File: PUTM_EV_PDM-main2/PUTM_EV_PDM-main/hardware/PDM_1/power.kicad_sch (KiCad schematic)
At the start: 21 parts, among them U2 LD1117S33TR_SOT223, U3 LM2675M-5

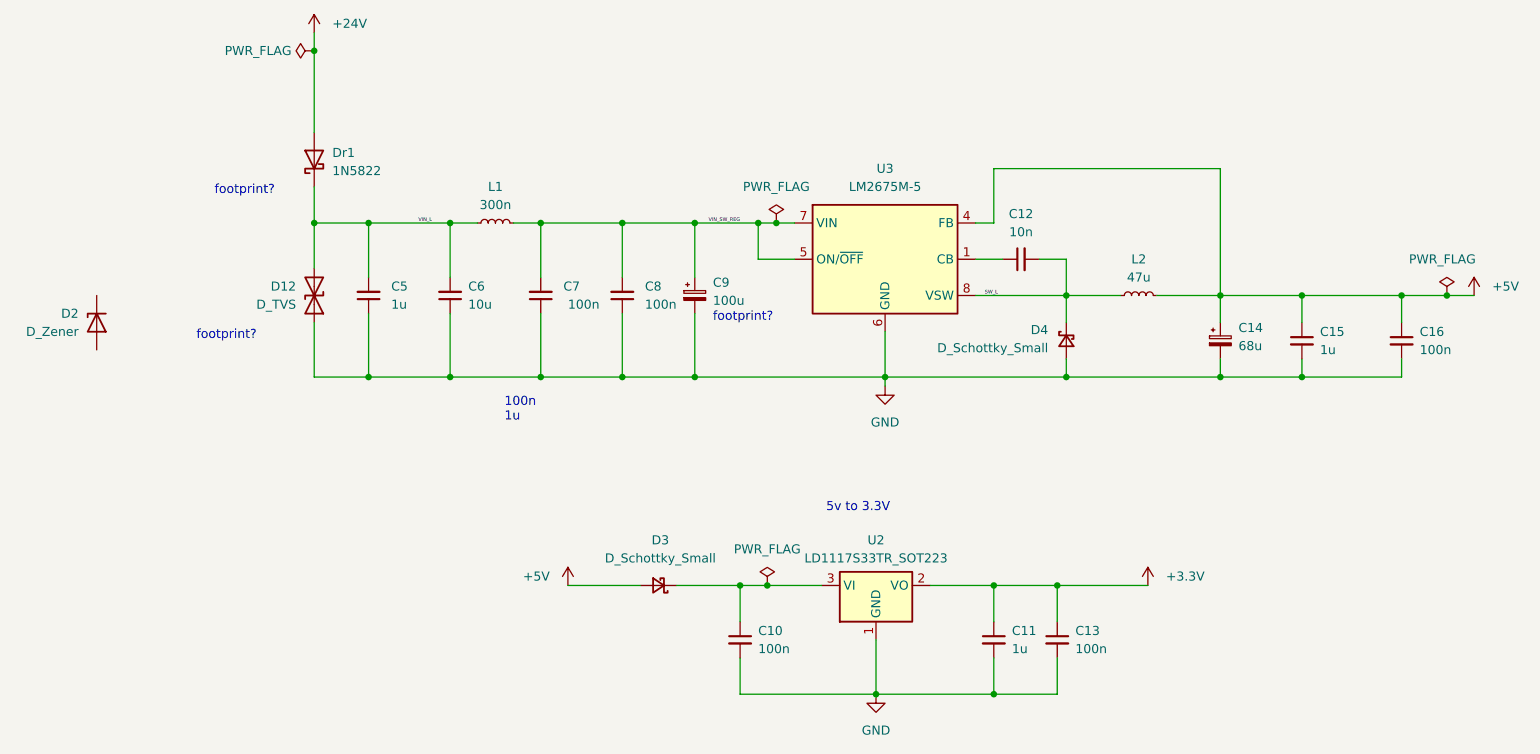
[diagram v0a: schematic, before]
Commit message: lepsze footprinty
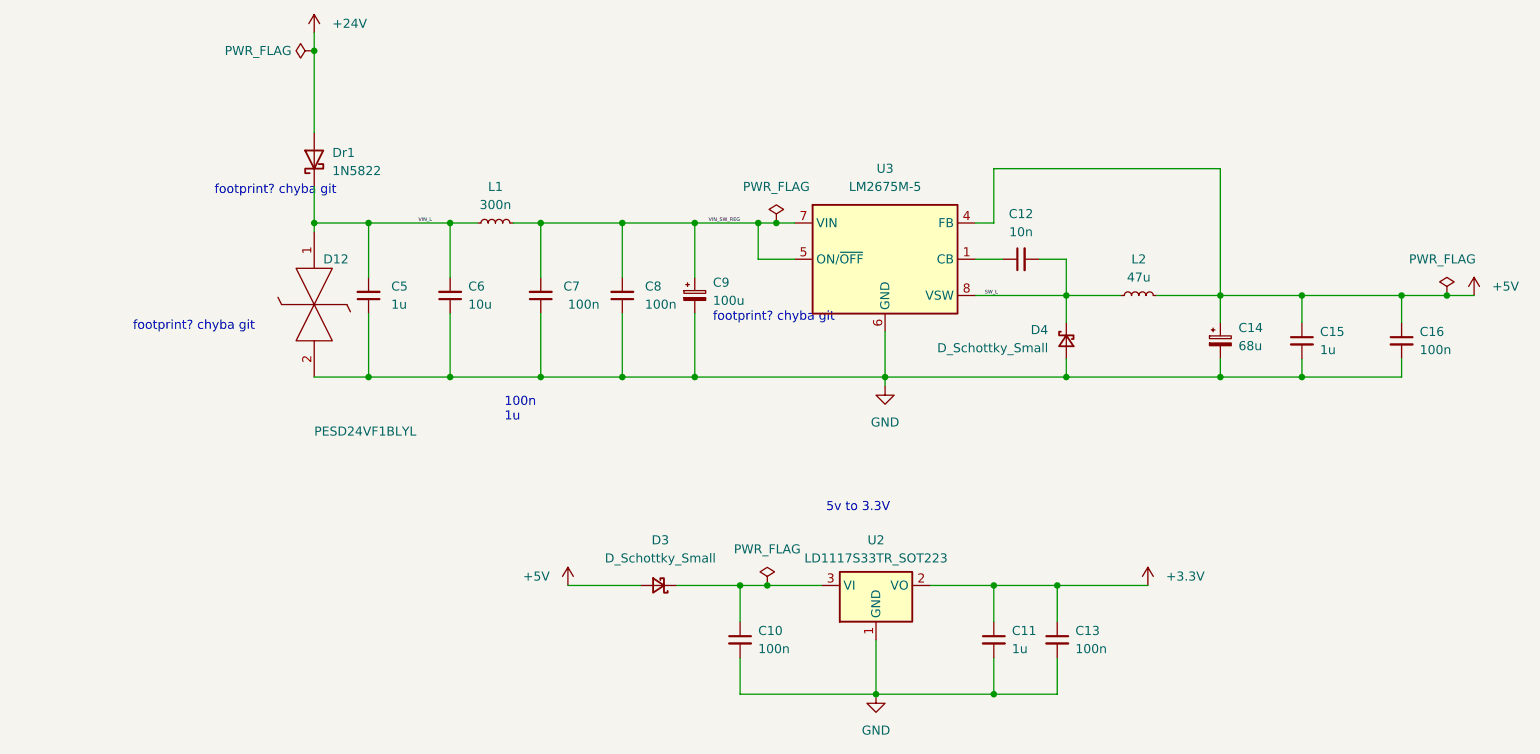
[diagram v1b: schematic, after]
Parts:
- removed D12: D_TVS, Diode_SMD:D_SMA, symbol Device:D_TVS
- removed D2: D_Zener, Diode_SMD:D_SOD-123, symbol Device:D_Zener
- added D12: PESD24VF1BLYL, Diode_SMD:D_SMA, symbol PESD24VF1BLYL:PESD24VF1BLYL
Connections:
- net GND: now also D12.2
- net VIN_L: now also D12.1
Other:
- note added: "footprint? chyba git"
- note removed: "footprint?"
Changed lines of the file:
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@@
   (junction (at 107.95 77.47) (diameter 0) (color 0 0 0 0)
   )
+  (junction (at 154.94 143.51) (diameter 0) (color 0 0 0 0)
+  )
+  (junction (at 129.54 99.06) (diameter 0) (color 0 0 0 0)
+  )
   (junction (at 76.2 77.47) (diameter 0) (color 0 0 0 0)
   )
-  (junction (at 154.94 143.51) (diameter 0) (color 0 0 0 0)
-  )
-  (junction (at 129.54 99.06) (diameter 0) (color 0 0 0 0)
-  )
   (junction (at 107.95 99.06) (diameter 0) (color 0 0 0 0)
   )
@@
     (stroke (width 0) (type default))
   )
+  (wire (pts (xy 76.2 77.47) (xy 76.2 78.74))
+    (stroke (width 0) (type default))
+  )
   (wire (pts (xy 119.38 77.47) (xy 129.54 77.47))
     (stroke (width 0) (type default))
@@
     (stroke (width 0) (type default))
   )
-  (wire (pts (xy 76.2 77.47) (xy 76.2 83.82))
-    (stroke (width 0) (type default))
-  )
   (wire (pts (xy 171.45 128.27) (xy 171.45 133.35))
     (stroke (width 0) (type default))
@@
     (stroke (width 0) (type default))
   )
-  (wire (pts (xy 76.2 91.44) (xy 76.2 99.06))
-    (stroke (width 0) (type default))
-  )
   (wire (pts (xy 83.82 90.17) (xy 83.82 99.06))
     (stroke (width 0) (type default))
@@
     (stroke (width 0) (type default))
   )
-  (text "footprint?" (at 59.69 93.98 0)
+  (text "footprint? chyba git" (at 50.8 92.71 0)
     (effects (font (size 1.27 1.27)) (justify left bottom))
   )
-  (text "footprint?" (at 132.08 91.44 0)
+  (text "footprint? chyba git\n" (at 132.08 91.44 0)
     (effects (font (size 1.27 1.27)) (justify left bottom))
   )
@@
     (effects (font (size 1.27 1.27)) (justify left bottom))
   )
-  (text "footprint?" (at 62.23 73.66 0)
+  (text "footprint? chyba git\n" (at 62.23 73.66 0)
     (effects (font (size 1.27 1.27)) (justify left bottom))
   )
@@
     )
   )
-  (symbol (lib_id "Device:D_Zener") (at 45.72 91.44 90) (mirror x) (unit 1)
+  (symbol (lib_id "power:+24V") (at 76.2 50.8 0) (unit 1)
+    (in_bom yes) (on_board yes) (dnp no) (fields_autoplaced)
+    (property "Reference" "#PWR04" (at 76.2 54.61 0)
+      (effects (font (size 1.27 1.27)) hide)
+    )
+    (property "Value" "+24V" (at 78.74 49.53 0)
+      (effects (font (size 1.27 1.27)) (justify left))
+    )
+    (property "Footprint" "" (at 76.2 50.8 0)
+      (effects (font (size 1.27 1.27)) hide)
+    )
+    (property "Datasheet" "" (at 76.2 50.8 0)
+      (effects (font (size 1.27 1.27)) hide)
+    )
+    (pin "1")
+    (instances
+      (project "PDM_1"
+        (path "/b652b05a-4e3d-4ad1-b032-18886abe7d45/1367ec17-5fee-46da-adec-17b799499894"
+          (reference "#PWR04") (unit 1)
+        )
+      )
+      (project "PDM"
+        (path "/d7434f1a-7415-4eaa-a71b-b9580d7b34f2/bce9111c-7679-44f6-9761-394d41af211c"
+          (reference "#PWR016") (unit 1)
+        )
+      )
+    )
+  )
+  (symbol (lib_id "PESD24VF1BLYL:PESD24VF1BLYL") (at 76.2 78.74 270) (unit 1)
     (in_bom yes) (on_board yes) (dnp no)
-    (property "Reference" "D2" (at 43.18 90.17 90)
-      (effects (font (size 1.27 1.27)) (justify left))
-    )
-    (property "Value" "D_Zener" (at 43.18 92.71 90)
-      (effects (font (size 1.27 1.27)) (justify left))
-    )
-    (property "Footprint" "Diode_SMD:D_SOD-123" (at 45.72 91.44 0)
-      (effects (font (size 1.27 1.27)) hide)
-    )
-    (property "Datasheet" "file:///C:/Users/kacpe/Downloads/1N4728A.PDF" (at 45.72 91.44 0)
-      (effects (font (size 1.27 1.27)) hide)
-    )
-    (pin "1")
-    (pin "2")
-    (instances
-      (project "PDM_1"
-        (path "/b652b05a-4e3d-4ad1-b032-18886abe7d45/1367ec17-5fee-46da-adec-17b799499894"
-          (reference "D2") (unit 1)
-        )
-      )
-      (project "PDM"
-        (path "/d7434f1a-7415-4eaa-a71b-b9580d7b34f2/bce9111c-7679-44f6-9761-394d41af211c"
-          (reference "D6") (unit 1)
-        )
-      )
-    )
-  )
-  (symbol (lib_id "power:+24V") (at 76.2 50.8 0) (unit 1)
-    (in_bom yes) (on_board yes) (dnp no) (fields_autoplaced)
-    (property "Reference" "#PWR04" (at 76.2 54.61 0)
-      (effects (font (size 1.27 1.27)) hide)
-    )
-    (property "Value" "+24V" (at 78.74 49.53 0)
-      (effects (font (size 1.27 1.27)) (justify left))
-    )
-    (property "Footprint" "" (at 76.2 50.8 0)
-      (effects (font (size 1.27 1.27)) hide)
-    )
-    (property "Datasheet" "" (at 76.2 50.8 0)
-      (effects (font (size 1.27 1.27)) hide)
-    )
-    (pin "1")
-    (instances
-      (project "PDM_1"
-        (path "/b652b05a-4e3d-4ad1-b032-18886abe7d45/1367ec17-5fee-46da-adec-17b799499894"
-          (reference "#PWR04") (unit 1)
-        )
-      )
-      (project "PDM"
-        (path "/d7434f1a-7415-4eaa-a71b-b9580d7b34f2/bce9111c-7679-44f6-9761-394d41af211c"
-          (reference "#PWR016") (unit 1)
+    (property "Reference" "D12" (at 77.47 82.55 90)
+      (effects (font (size 1.27 1.27)) (justify left))
+    )
+    (property "Value" "PESD24VF1BLYL" (at 76.2 106.68 90)
+      (effects (font (size 1.27 1.27)) (justify left))
+    )
+    (property "Footprint" "Diode_SMD:D_SMA" (at 80.01 93.98 0)
+      (effects (font (size 1.27 1.27)) (justify left bottom) hide)
+    )
+    (property "Datasheet" "https://assets.nexperia.com/documents/data-sheet/PESD24VF1BL.pdf" (at 77.47 93.98 0)
+      (effects (font (size 1.27 1.27)) (justify left bottom) hide)
+    )
+    (property "Description" "PESD24VF1BL - Ultra low capacitance bidirectional ESD protection diode" (at 74.93 93.98 0)
+      (effects (font (size 1.27 1.27)) (justify left bottom) hide)
+    )
+    (property "Height" "0" (at 72.39 93.98 0)
+      (effects (font (size 1.27 1.27)) (justify left bottom) hide)
+    )
+    (property "Mouser Part Number" "771-PESD24VF1BLYL" (at 69.85 93.98 0)
+      (effects (font (size 1.27 1.27)) (justify left bottom) hide)
+    )
+    (property "Mouser Price/Stock" "https://www.mouser.co.uk/ProductDetail/Nexperia/PESD24VF1BLYL?qs=M%2FOdCRO8QQ2u4QQQVkgemw%3D%3D" (at 67.31 93.98 0)
+      (effects (font (size 1.27 1.27)) (justify left bottom) hide)
+    )
+    (property "Manufacturer_Name" "Nexperia" (at 64.77 93.98 0)
+      (effects (font (size 1.27 1.27)) (justify left bottom) hide)
+    )
+    (property "Manufacturer_Part_Number" "PESD24VF1BLYL" (at 62.23 93.98 0)
+      (effects (font (size 1.27 1.27)) (justify left bottom) hide)
+    )
+    (pin "1")
+    (pin "2")
+    (instances
+      (project "PDM_1"
+        (path "/b652b05a-4e3d-4ad1-b032-18886abe7d45/1367ec17-5fee-46da-adec-17b799499894"
+          (reference "D12") (unit 1)
         )
       )
@@
     )
   )
-  (symbol (lib_id "Device:D_TVS") (at 76.2 87.63 270) (mirror x) (unit 1)
-    (in_bom yes) (on_board yes) (dnp no)
-    (property "Reference" "D12" (at 73.66 86.36 90)
-      (effects (font (size 1.27 1.27)) (justify right))
-    )
-    (property "Value" "D_TVS" (at 73.66 88.9 90)
-      (effects (font (size 1.27 1.27)) (justify right))
-    )
-    (property "Footprint" "Diode_SMD:D_SMA" (at 76.2 87.63 0)
-      (effects (font (size 1.27 1.27)) hide)
-    )
-    (property "Datasheet" "~" (at 76.2 87.63 0)
-      (effects (font (size 1.27 1.27)) hide)
-    )
-    (pin "1")
-    (pin "2")
-    (instances
-      (project "PDM_1"
-        (path "/b652b05a-4e3d-4ad1-b032-18886abe7d45/1367ec17-5fee-46da-adec-17b799499894"
-          (reference "D12") (unit 1)
-        )
-      )
-    )
-  )
   (symbol (lib_id "power:PWR_FLAG") (at 76.2 53.34 90) (unit 1)
     (in_bom yes) (on_board yes) (dnp no) (fields_autoplaced)
@@
       (effects (font (size 1.27 1.27)) hide)
     )
-    (property "Datasheet" "http://www.vishay.com/docs/88526/1n5820.pdf" (at 76.2 68.58 0)
-      (effects (font (size 1.27 1.27)) hide)
-    )
+    (property "Datasheet" "https://www.mouser.pl/ProductDetail/Taiwan-Semiconductor/SS34ALH?qs=A6eO%252BMLsxmQip%2FrgNup6RA%3D%3D" (at 76.2 68.58 0)
+      (effects (font (size 1.27 1.27)) hide)
+    )

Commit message: nowe połączenia
dodane połączenia z STM
dodane złącza
dodane LED
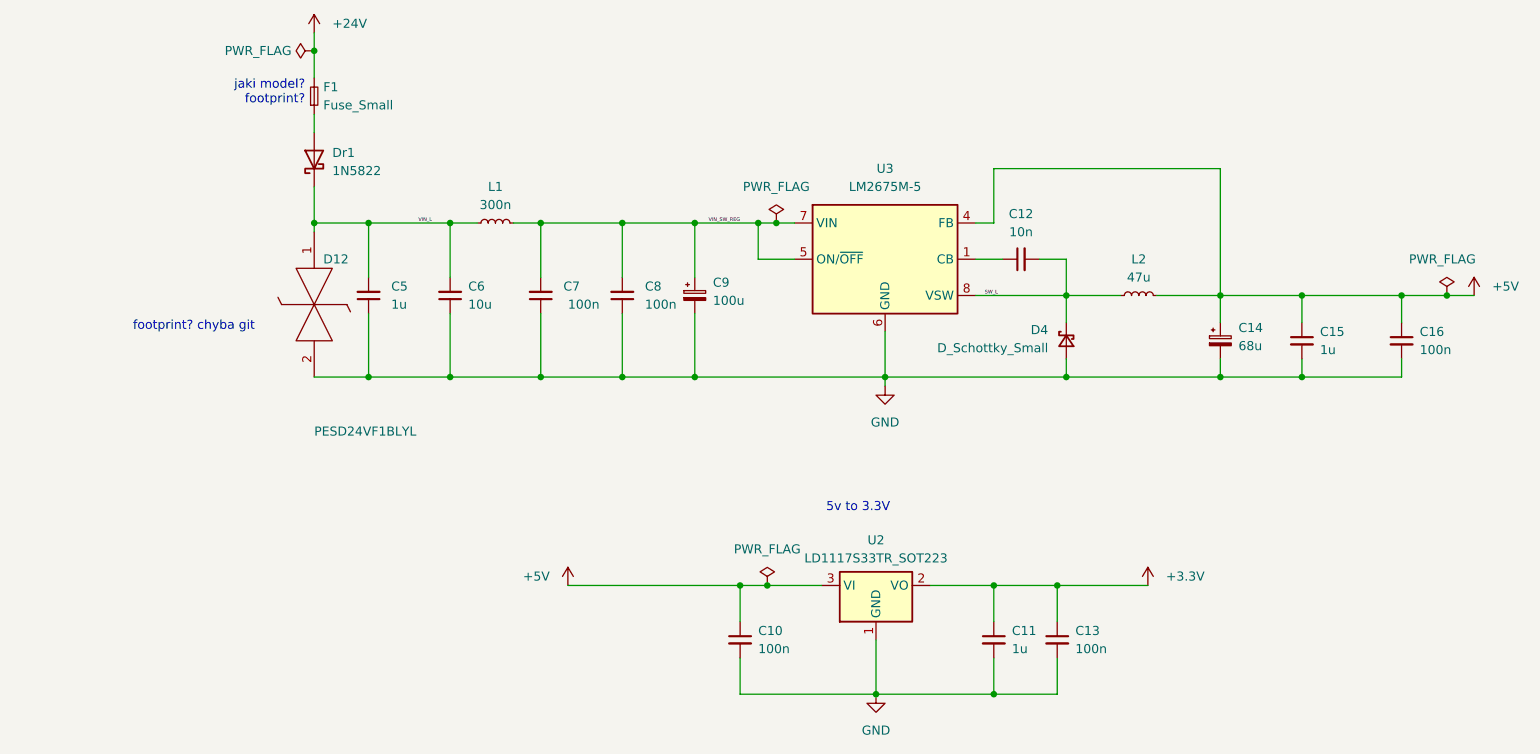
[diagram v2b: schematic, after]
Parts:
- removed D3: D_Schottky_Small, Diode_SMD:D_SOD-123, symbol Device:D_Schottky_Small
- added F1: Fuse_Small, symbol Device:Fuse_Small
- C14: footprint Capacitor_SMD:CP_Elec_6.3x7.7 -> Capacitor_SMD:CP_Elec_6.3x5.5
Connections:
- net +24V: now also F1.2; no longer Dr1.2 (A)
- net +5V: now also C10.1, U2.3 (VI)
- new net: Dr1.2 (A), F1.1
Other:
- note added: "jaki model? footprint?"
- note removed: "100n 1u"
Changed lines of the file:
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@@
+    (stroke (width 0) (type default))
+  )
+  (wire (pts (xy 76.2 62.23) (xy 76.2 64.77))
     (stroke (width 0) (type default))
   )
@@
     (stroke (width 0) (type default))
   )
-  (wire (pts (xy 111.76 128.27) (xy 121.92 128.27))
-    (stroke (width 0) (type default))
-  )
   (wire (pts (xy 95.25 99.06) (xy 107.95 99.06))
     (stroke (width 0) (type default))
@@
     (stroke (width 0) (type default))
   )
-  (wire (pts (xy 127 128.27) (xy 135.89 128.27))
+  (wire (pts (xy 111.76 128.27) (xy 135.89 128.27))
     (stroke (width 0) (type default))
   )
@@
     (stroke (width 0) (type default))
   )
-  (wire (pts (xy 76.2 53.34) (xy 76.2 64.77))
+  (wire (pts (xy 76.2 53.34) (xy 76.2 57.15))
     (stroke (width 0) (type default))
   )
@@
     (effects (font (size 1.27 1.27)) (justify left bottom))
   )
-  (text "footprint? chyba git\n" (at 132.08 91.44 0)
-    (effects (font (size 1.27 1.27)) (justify left bottom))
+  (text "jaki model?\nfootprint?\n" (at 74.93 60.96 0)
+    (effects (font (size 1.27 1.27)) (justify right bottom))
   )
   (text "5v to 3.3V" (at 147.955 118.11 0)
-    (effects (font (size 1.27 1.27)) (justify left bottom))
-  )
-  (text "footprint? chyba git\n" (at 62.23 73.66 0)
-    (effects (font (size 1.27 1.27)) (justify left bottom))
-  )
-  (text "100n\n1u " (at 102.87 105.41 0)
     (effects (font (size 1.27 1.27)) (justify left bottom))
   )
@@
       (effects (font (size 1.27 1.27)) (justify left))
     )
-    (property "Footprint" "Capacitor_SMD:CP_Elec_6.3x7.7" (at 203.2 93.98 0)
-      (effects (font (size 1.27 1.27)) hide)
-    )
-    (property "Datasheet" "https://www.mouser.pl/ProductDetail/Vishay-Sprague/293D686X9010D2TE3?qs=gJz7vFReE9iU4aBFRHLukg%3D%3D" (at 203.2 93.98 0)
+    (property "Footprint" "Capacitor_SMD:CP_Elec_6.3x5.5" (at 203.2 93.98 0)
+      (effects (font (size 1.27 1.27)) hide)
+    )
+    (property "Datasheet" "https://www.mouser.pl/ProductDetail/Wurth-Elektronik/865080243006?qs=0KOYDY2FL2%252Bzh3fs6MlnCA%3D%3D" (at 203.2 93.98 0)
       (effects (font (size 1.27 1.27)) hide)
     )
@@
     )
   )
-  (symbol (lib_id "Device:D_Schottky_Small") (at 124.46 128.27 180) (unit 1)
-    (in_bom yes) (on_board yes) (dnp no) (fields_autoplaced)
-    (property "Reference" "D3" (at 124.714 121.92 0)
-      (effects (font (size 1.27 1.27)))
-    )
-    (property "Value" "D_Schottky_Small" (at 124.714 124.46 0)
-      (effects (font (size 1.27 1.27)))
-    )
-    (property "Footprint" "Diode_SMD:D_SOD-123" (at 124.46 128.27 90)
-      (effects (font (size 1.27 1.27)) hide)
-    )
-    (property "Datasheet" "~" (at 124.46 128.27 90)
-      (effects (font (size 1.27 1.27)) hide)
-    )
-    (pin "2")
-    (pin "1")
-    (instances
-      (project "PDM_1"
-        (path "/b652b05a-4e3d-4ad1-b032-18886abe7d45/1367ec17-5fee-46da-adec-17b799499894"
-          (reference "D3") (unit 1)
-        )
-      )
-      (project "PDM"
-        (path "/d7434f1a-7415-4eaa-a71b-b9580d7b34f2/bce9111c-7679-44f6-9761-394d41af211c"
-          (reference "D7") (unit 1)
-        )
-      )
-    )
-  )
   (symbol (lib_id "power:GND") (at 154.94 143.51 0) (unit 1)
     (in_bom yes) (on_board yes) (dnp no) (fields_autoplaced)
@@
         )
       )
+    )
+  )
+  (symbol (lib_id "Device:Fuse_Small") (at 76.2 59.69 90) (unit 1)
+    (in_bom yes) (on_board yes) (dnp no) (fields_autoplaced)
+    (property "Reference" "F1" (at 77.47 58.42 90)
+      (effects (font (size 1.27 1.27)) (justify right))
+    )
+    (property "Value" "Fuse_Small" (at 77.47 60.96 90)
+      (effects (font (size 1.27 1.27)) (justify right))
+    )
+    (property "Footprint" "" (at 76.2 59.69 0)
+      (effects (font (size 1.27 1.27)) hide)
+    )
+    (property "Datasheet" "~" (at 76.2 59.69 0)
+      (effects (font (size 1.27 1.27)) hide)
+    )
+    (pin "2")
+    (pin "1")
+    (instances
+      (project "PDM_1"
+        (path "/b652b05a-4e3d-4ad1-b032-18886abe7d45/1367ec17-5fee-46da-adec-17b799499894"
+          (reference "F1") (unit 1)
+        )
+      )
